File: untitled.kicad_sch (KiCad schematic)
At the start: 5 parts, among them J1 Antenna SMA, J2 DB15_Female, J3 Screw_Terminal_01x08, J4 Screw_Terminal_01x12

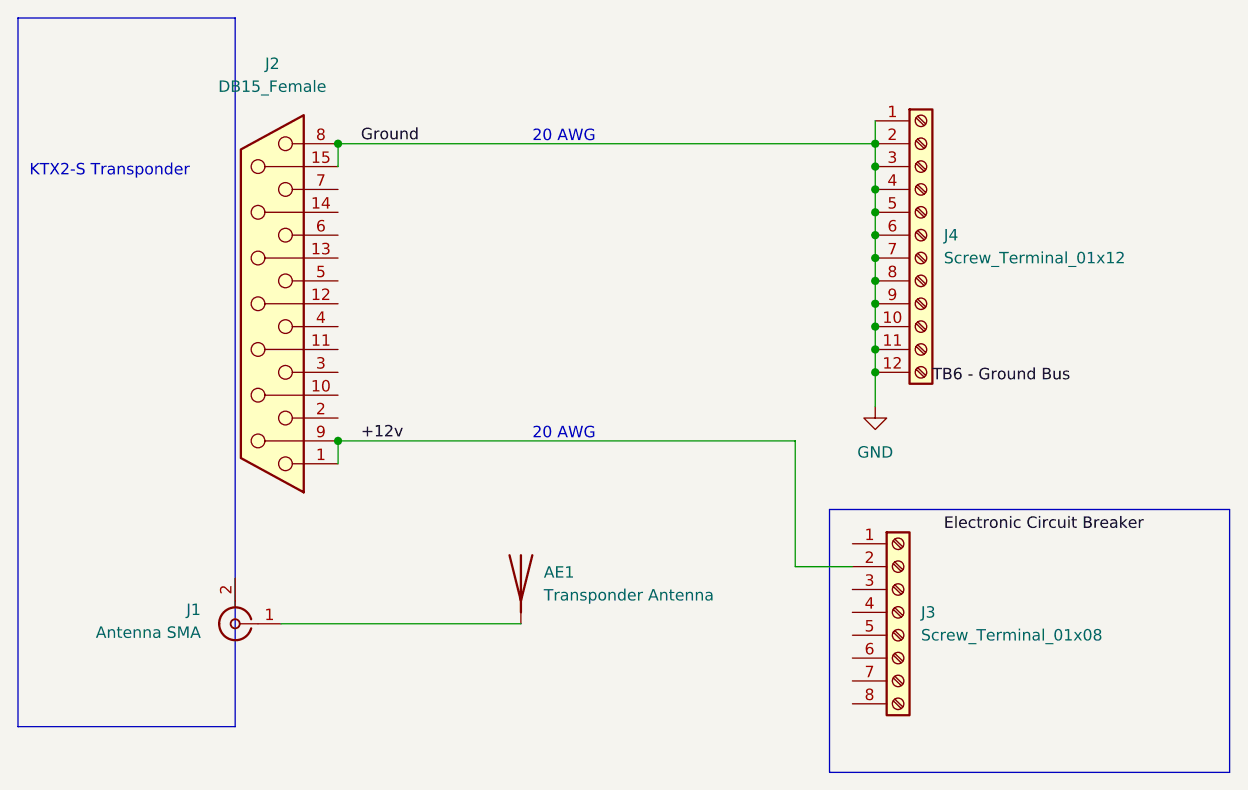
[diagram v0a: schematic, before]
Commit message: Added regulator sheet
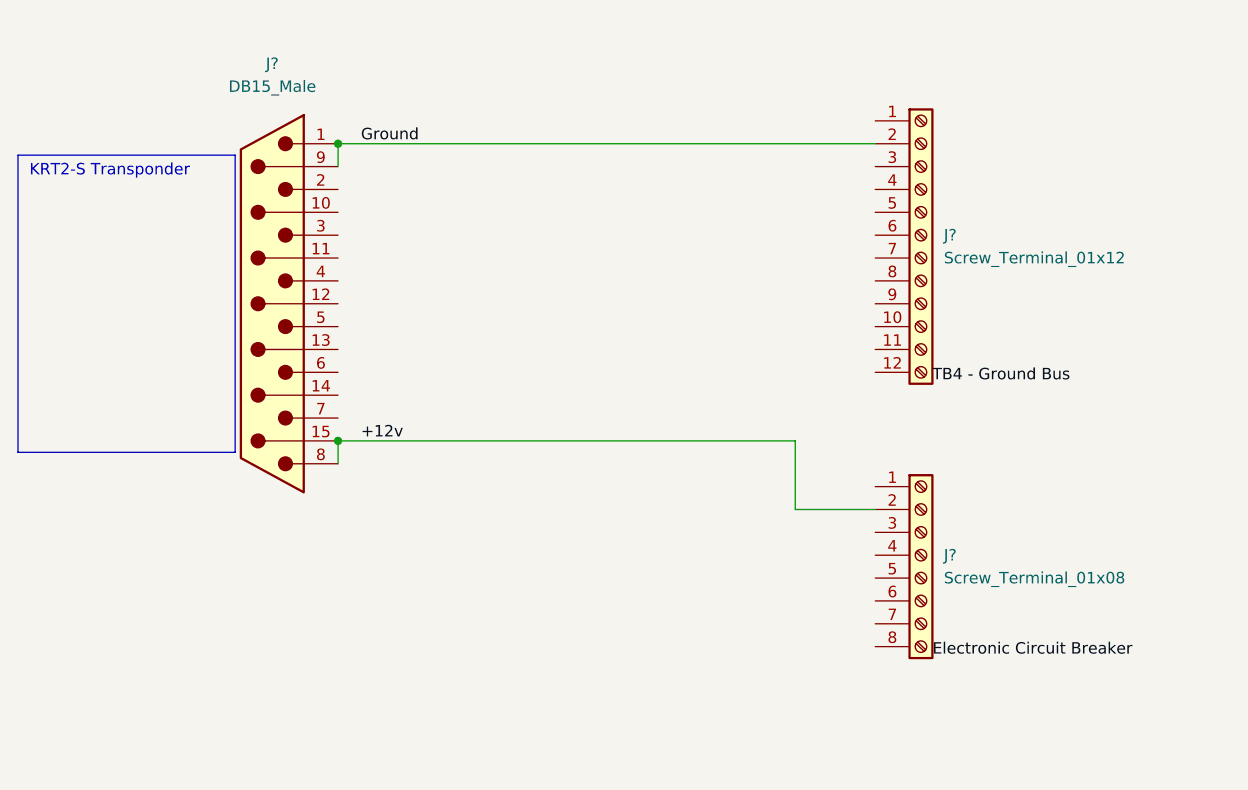
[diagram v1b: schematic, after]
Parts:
- removed AE1: Transponder Antenna, symbol Device:Antenna
- removed J1: Antenna SMA, symbol Connector:Conn_Coaxial
- J?: renamed from J2; value DB15_Female -> DB15_Male; symbol Connector:DB15_Female -> Connector:DB15_Male
- renumbered J4 to J?, J3 to J?
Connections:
- net +12v: now also J?.15 (P15), J?.8; no longer J?.1, J?.9 (P9)
- removed net GND: J?.1 (Pin_1), J?.10 (Pin_10), J?.11 (Pin_11), J?.12 (Pin_12), J?.15 (P15), J?.2 (Pin_2), J?.3 (Pin_3), J?.4 (Pin_4), J?.5 (Pin_5), J?.6 (Pin_6), J?.7 (Pin_7), J?.8, J?.8 (Pin_8), J?.9 (Pin_9)
- new net Ground: J?.1, J?.2 (Pin_2), J?.9 (P9)
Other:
- note added: "KRT2-S Transponder"
- note removed: "20 AWG"
- note removed: "KTX2-S Transponder"
- title: Europa Transponder -> (none)
- moved on the sheet: J?
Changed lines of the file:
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@@
 (kicad_sch (version 20211123) (generator eeschema)
   (paper "A4")
-  (title_block
-    (title "Europa Transponder")
-    (date "2022-11-24")
-    (rev "4")
-    (comment 1 "Comment 1")
-  )
-  (junction (at 180.34 63.5) (diameter 0) (color 0 0 0 0)
-  )
-  (junction (at 180.34 83.82) (diameter 0) (color 0 0 0 0)
-  )
-  (junction (at 180.34 60.96) (diameter 0) (color 0 0 0 0)
-  )
-  (junction (at 180.34 68.58) (diameter 0) (color 0 0 0 0)
-  )
-  (junction (at 180.34 78.74) (diameter 0) (color 0 0 0 0)
-  )
-  (junction (at 180.34 58.42) (diameter 0) (color 0 0 0 0)
-  )
-  (junction (at 180.34 81.28) (diameter 0) (color 0 0 0 0)
-  )
   (junction (at 120.65 58.42) (diameter 0) (color 0 0 0 0)
-  )
-  (junction (at 180.34 76.2) (diameter 0) (color 0 0 0 0)
-  )
-  (junction (at 180.34 73.66) (diameter 0) (color 0 0 0 0)
   )
   (junction (at 120.65 91.44) (diameter 0) (color 0 0 0 0)
   )
-  (junction (at 180.34 71.12) (diameter 0) (color 0 0 0 0)
-  )
-  (junction (at 180.34 66.04) (diameter 0) (color 0 0 0 0)
-  )
-  (polyline (pts (xy 85.09 44.45) (xy 85.09 123.19))
-    (stroke (width 0) (type default) (color 0 0 0 0))
-  )
-  (wire (pts (xy 180.34 83.82) (xy 180.34 87.63))
-    (stroke (width 0) (type default) (color 0 0 0 0))
-  )
-  (wire (pts (xy 180.34 78.74) (xy 180.34 81.28))
-    (stroke (width 0) (type default) (color 0 0 0 0))
-  )
-  (wire (pts (xy 180.34 81.28) (xy 180.34 83.82))
+  (polyline (pts (xy 85.09 59.69) (xy 85.09 92.71))
     (stroke (width 0) (type default) (color 0 0 0 0))
   )
@@
     (stroke (width 0) (type default) (color 0 0 0 0))
   )
-  (polyline (pts (xy 85.09 123.19) (xy 109.22 123.19))
+  (polyline (pts (xy 85.09 92.71) (xy 109.22 92.71))
     (stroke (width 0) (type default) (color 0 0 0 0))
   )
@@
     (stroke (width 0) (type default) (color 0 0 0 0))
   )
-  (wire (pts (xy 180.34 58.42) (xy 180.34 60.96))
+  (polyline (pts (xy 109.22 59.69) (xy 85.09 59.69))
     (stroke (width 0) (type default) (color 0 0 0 0))
   )
-  (polyline (pts (xy 109.22 44.45) (xy 85.09 44.45))
+  (polyline (pts (xy 109.22 59.69) (xy 109.22 92.71))
     (stroke (width 0) (type default) (color 0 0 0 0))
   )
-  (wire (pts (xy 180.34 73.66) (xy 180.34 76.2))
+  (wire (pts (xy 171.45 99.06) (xy 180.34 99.06))
     (stroke (width 0) (type default) (color 0 0 0 0))
   )
-  (wire (pts (xy 180.34 55.88) (xy 180.34 58.42))
-    (stroke (width 0) (type default) (color 0 0 0 0))
-  )
-  (polyline (pts (xy 109.22 44.45) (xy 109.22 123.19))
-    (stroke (width 0) (type default) (color 0 0 0 0))
-  )
-  (polyline (pts (xy 175.26 99.06) (xy 219.71 99.06))
-    (stroke (width 0) (type default) (color 0 0 0 0))
-  )
-  (wire (pts (xy 180.34 60.96) (xy 180.34 63.5))
-    (stroke (width 0) (type default) (color 0 0 0 0))
-  )
-  (wire (pts (xy 171.45 91.44) (xy 171.45 105.41))
-    (stroke (width 0) (type default) (color 0 0 0 0))
-  )
-  (wire (pts (xy 180.34 68.58) (xy 180.34 71.12))
-    (stroke (width 0) (type default) (color 0 0 0 0))
-  )
-  (polyline (pts (xy 219.71 128.27) (xy 175.26 128.27))
-    (stroke (width 0) (type default) (color 0 0 0 0))
-  )
-  (wire (pts (xy 180.34 71.12) (xy 180.34 73.66))
-    (stroke (width 0) (type default) (color 0 0 0 0))
-  )
-  (polyline (pts (xy 219.71 99.06) (xy 219.71 128.27))
-    (stroke (width 0) (type default) (color 0 0 0 0))
-  )
-  (wire (pts (xy 114.3 111.76) (xy 140.97 111.76))
+  (wire (pts (xy 171.45 91.44) (xy 171.45 99.06))
     (stroke (width 0) (type default) (color 0 0 0 0))
   )
@@
     (stroke (width 0) (type default) (color 0 0 0 0))
   )
-  (wire (pts (xy 171.45 105.41) (xy 177.8 105.41))
-    (stroke (width 0) (type default) (color 0 0 0 0))
-  )
   (wire (pts (xy 120.65 58.42) (xy 180.34 58.42))
     (stroke (width 0) (type default) (color 0 0 0 0))
   )
-  (wire (pts (xy 180.34 66.04) (xy 180.34 68.58))
-    (stroke (width 0) (type default) (color 0 0 0 0))
-  )
-  (wire (pts (xy 180.34 76.2) (xy 180.34 78.74))
-    (stroke (width 0) (type default) (color 0 0 0 0))
-  )
-  (wire (pts (xy 180.34 63.5) (xy 180.34 66.04))
-    (stroke (width 0) (type default) (color 0 0 0 0))
-  )
-  (polyline (pts (xy 175.26 99.06) (xy 175.26 128.27))
-    (stroke (width 0) (type default) (color 0 0 0 0))
-  )
-  (text "20 AWG" (at 142.24 58.42 0)
+  (text "KRT2-S Transponder" (at 86.36 62.23 0)
     (effects (font (size 1.27 1.27)) (justify left bottom))
   )
-  (text "20 AWG" (at 142.24 91.44 0)
-    (effects (font (size 1.27 1.27)) (justify left bottom))
-  )
-  (text "KTX2-S Transponder" (at 86.36 62.23 0)
-    (effects (font (size 1.27 1.27)) (justify left bottom))
-  )
-  (label "Electronic Circuit Breaker" (at 187.96 101.6 0)
+  (label "Electronic Circuit Breaker" (at 186.69 115.57 0)
     (effects (font (size 1.27 1.27)) (justify left bottom))
   )
@@
     (effects (font (size 1.27 1.27)) (justify left bottom))
   )
-  (label "TB6 - Ground Bus" (at 186.69 85.09 0)
+  (label "TB4 - Ground Bus" (at 186.69 85.09 0)
     (effects (font (size 1.27 1.27)) (justify left bottom))
   )
   (symbol (lib_id "Connector:Screw_Terminal_01x12") (at 185.42 68.58 0) (unit 1)
     (in_bom yes) (on_board yes) (fields_autoplaced)
-    (property "Reference" "J4" (id 0) (at 187.96 68.5799 0)
+    (property "Reference" "J?" (id 0) (at 187.96 68.5799 0)
       (effects (font (size 1.27 1.27)) (justify left))
     )
@@
     (pin "9")
   )
-  (symbol (lib_id "Connector:Screw_Terminal_01x08") (at 182.88 110.49 0) (unit 1)
+  (symbol (lib_id "Connector:Screw_Terminal_01x08") (at 185.42 104.14 0) (unit 1)
     (in_bom yes) (on_board yes) (fields_autoplaced)
-    (property "Reference" "J3" (id 0) (at 185.42 110.4899 0)
+    (property "Reference" "J?" (id 0) (at 187.96 104.1399 0)
       (effects (font (size 1.27 1.27)) (justify left))
     )
-    (property "Value" "Screw_Terminal_01x08" (id 1) (at 185.42 113.0299 0)
+    (property "Value" "Screw_Terminal_01x08" (id 1) (at 187.96 106.6799 0)
       (effects (font (size 1.27 1.27)) (justify left))
     )
-    (property "Footprint" "" (id 2) (at 182.88 110.49 0)
+    (property "Footprint" "" (id 2) (at 185.42 104.14 0)
       (effects (font (size 1.27 1.27)) hide)
     )
-    (property "Datasheet" "~" (id 3) (at 182.88 110.49 0)
+    (property "Datasheet" "~" (id 3) (at 185.42 104.14 0)
       (effects (font (size 1.27 1.27)) hide)
     )
@@
     (pin "8")
   )
-  (symbol (lib_id "Device:Antenna") (at 140.97 106.68 0) (unit 1)
+  (symbol (lib_id "Connector:DB15_Male") (at 113.03 76.2 180) (unit 1)
     (in_bom yes) (on_board yes) (fields_autoplaced)
-    (property "Reference" "AE1" (id 0) (at 143.51 106.0449 0)
-      (effects (font (size 1.27 1.27)) (justify left))
-    )
-    (property "Value" "Transponder Antenna" (id 1) (at 143.51 108.5849 0)
-      (effects (font (size 1.27 1.27)) (justify left))
-    )
-    (property "Footprint" "" (id 2) (at 140.97 106.68 0)
-      (effects (font (size 1.27 1.27)) hide)
-    )
-    (property "Datasheet" "~" (id 3) (at 140.97 106.68 0)
-      (effects (font (size 1.27 1.27)) hide)
-    )
-    (pin "1")
-  )
-  (symbol (lib_id "Connector:Conn_Coaxial") (at 109.22 111.76 180) (unit 1)
-    (in_bom yes) (on_board yes) (fields_autoplaced)
-    (property "Reference" "J1" (id 0) (at 105.41 110.1967 0)
-      (effects (font (size 1.27 1.27)) (justify left))
-    )
-    (property "Value" "Antenna SMA" (id 1) (at 105.41 112.7367 0)
-      (effects (font (size 1.27 1.27)) (justify left))
-    )
-    (property "Footprint" "" (id 2) (at 109.22 111.76 0)
-      (effects (font (size 1.27 1.27)) hide)
-    )
-    (property "Datasheet" " ~" (id 3) (at 109.22 111.76 0)
-      (effects (font (size 1.27 1.27)) hide)
-    )
-    (pin "1")
-    (pin "2")
-  )
-  (symbol (lib_id "Connector:DB15_Female") (at 113.03 76.2 180) (unit 1)
-    (in_bom yes) (on_board yes) (fields_autoplaced)
-    (property "Reference" "J2" (id 0) (at 113.3475 49.53 0))
-    (property "Value" "DB15_Female" (id 1) (at 113.3475 52.07 0))
+    (property "Reference" "J?" (id 0) (at 113.3475 49.53 0))
+    (property "Value" "DB15_Male" (id 1) (at 113.3475 52.07 0))
     (property "Footprint" "" (id 2) (at 113.03 76.2 0)
       (effects (font (size 1.27 1.27)) hide)
@@
     (pin "9")
   )
-  (symbol (lib_id "power:GND") (at 180.34 87.63 0) (unit 1)
-    (in_bom yes) (on_board yes) (fields_autoplaced)
-    (property "Reference" "#PWR01" (id 0) (at 180.34 93.98 0)
-      (effects (font (size 1.27 1.27)) hide)
-    )
-    (property "Value" "GND" (id 1) (at 180.34 92.71 0))
-    (property "Footprint" "" (id 2) (at 180.34 87.63 0)
-      (effects (font (size 1.27 1.27)) hide)
-    )
-    (property "Datasheet" "" (id 3) (at 180.34 87.63 0)
-      (effects (font (size 1.27 1.27)) hide)
-    )
-    (pin "1")
-  )
 )
